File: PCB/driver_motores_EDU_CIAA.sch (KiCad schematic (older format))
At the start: 37 parts, among them P1 CONN_01X02, P2 CONN_01X04, P3 CONN_01X05, P4 CONN_01X05, Q1 AOD417, U1 PCA9685-TSSOP, U2 24C32, U3 TB6612FNG, U4 TB6612FNG

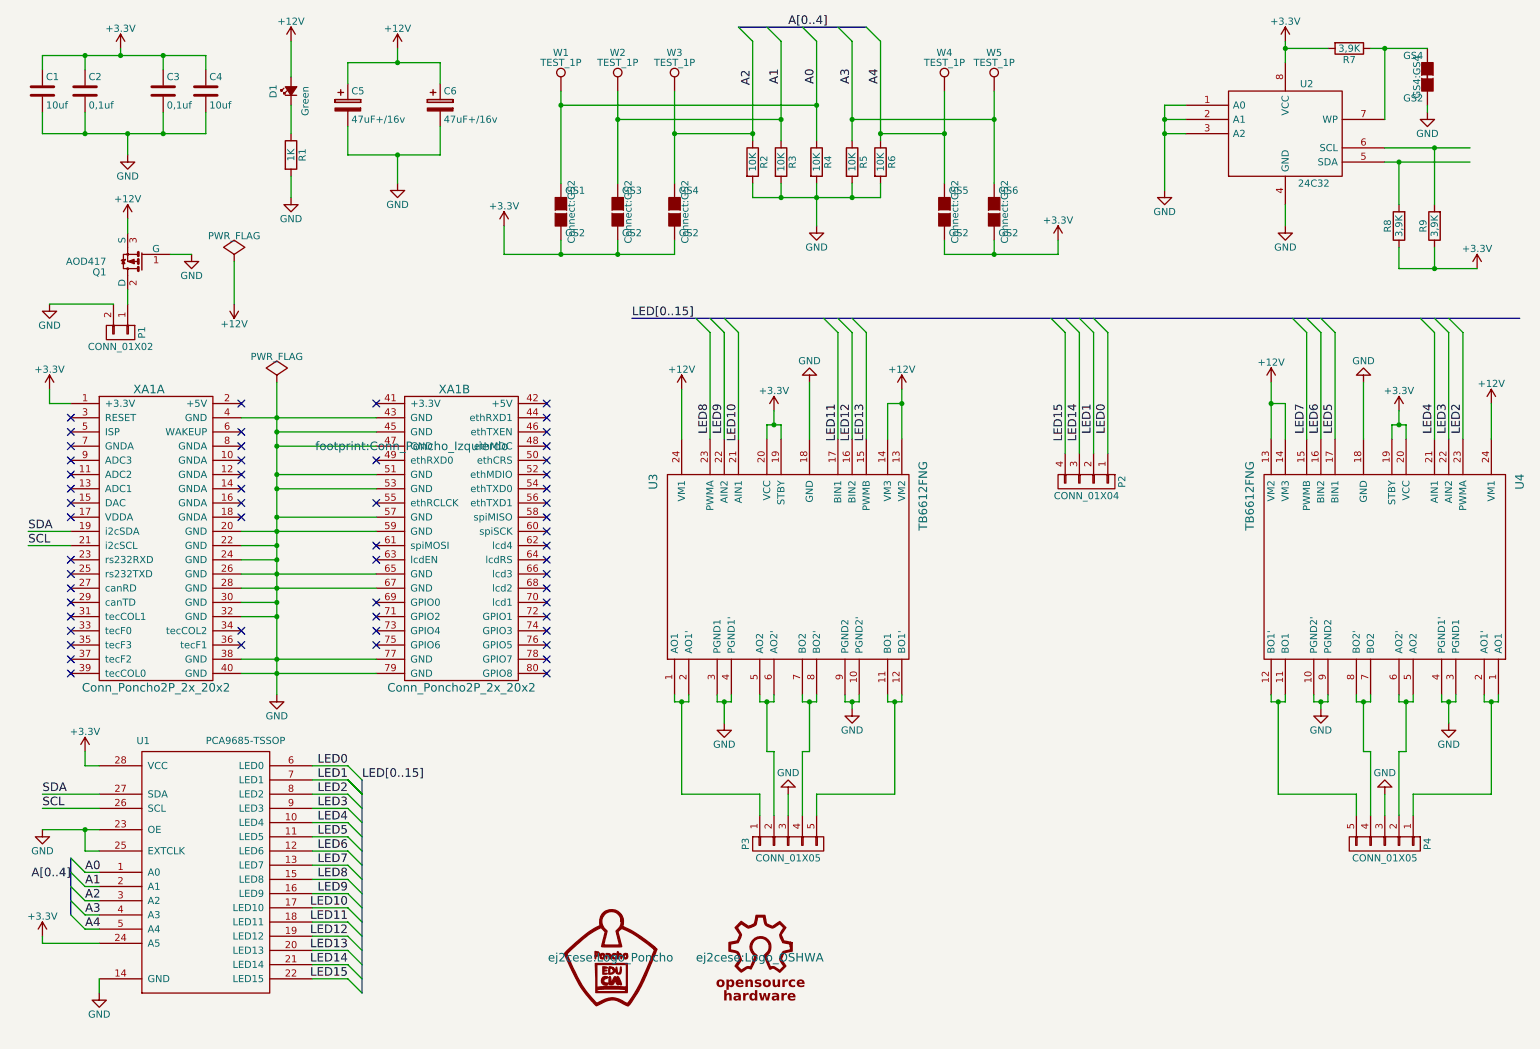
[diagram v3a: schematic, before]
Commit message: se borran las carpetas sobrantes, completa el rotulo, se corrige el esquematico, se agrega serigrafia, se agrega tabla con las grillas
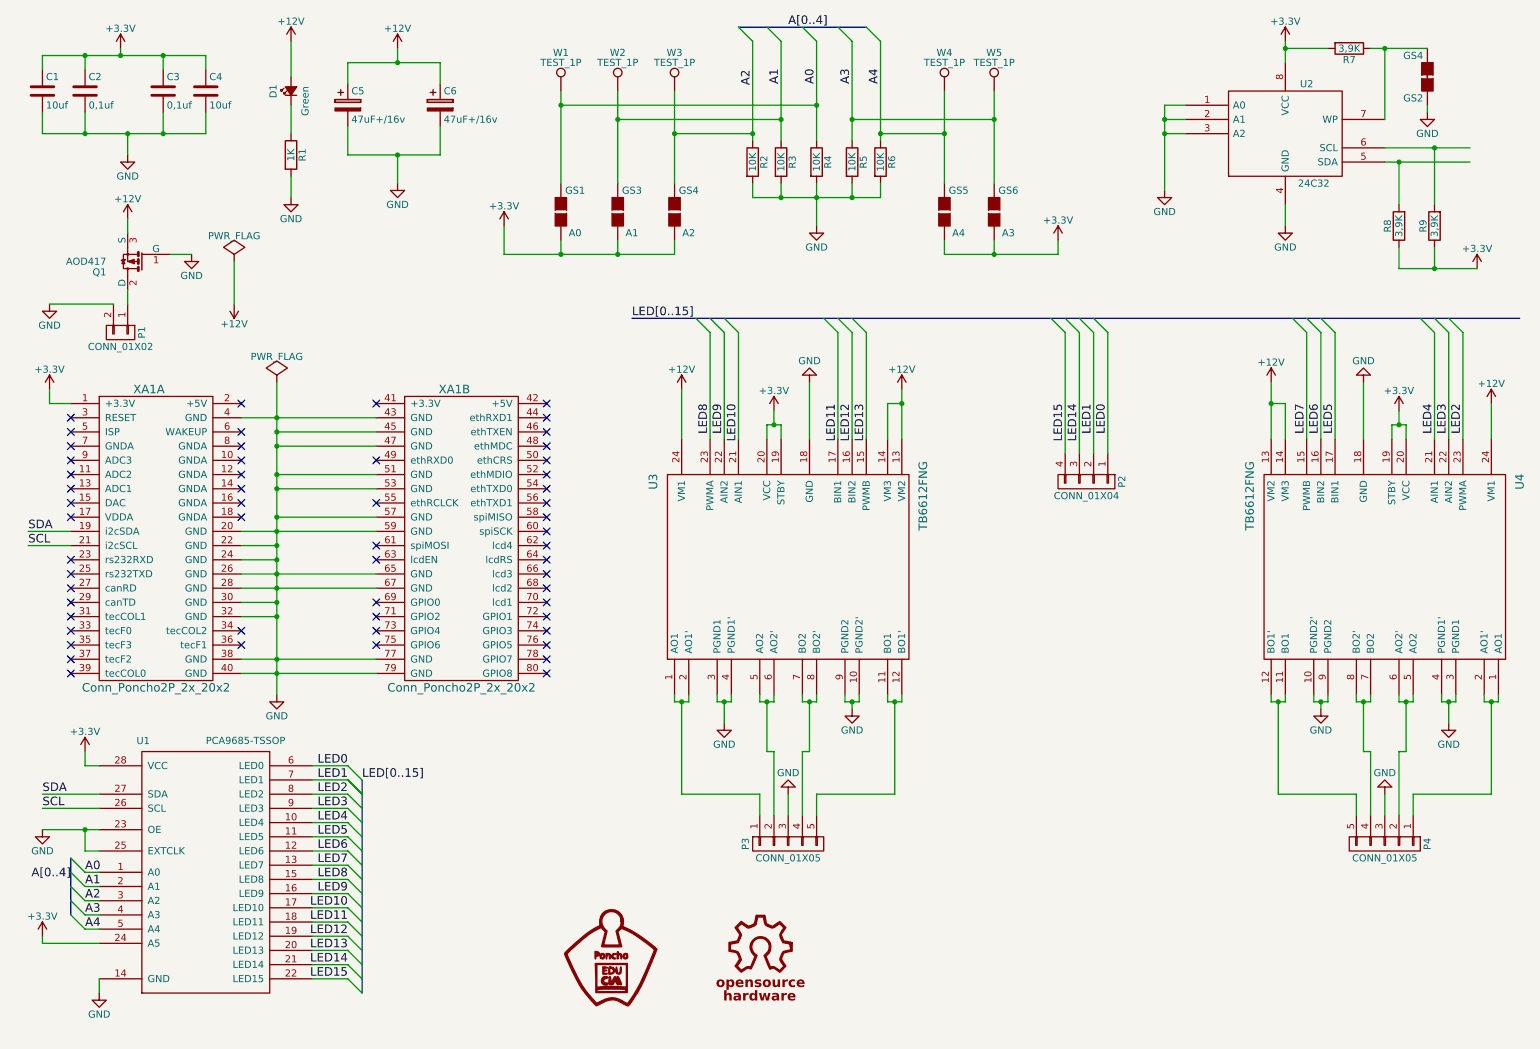
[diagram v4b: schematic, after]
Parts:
- GS1: value GS2 -> A0
- GS3: value GS2 -> A1
- GS4: value GS2 -> A2
- GS5: value GS2 -> A4
- GS6: value GS2 -> A3
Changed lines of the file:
@@
 encoding utf-8
 Sheet 1 1
-Title "Poncho punete H por i2C "
-Date "2016-12-13"
-Rev "1.2"
+Title "Poncho puente H por i2C "
+Date "2016-12-22"
+Rev "1.3"
 Comp "Martinez Horacio"
 Comment1 "Revisor: Guillermo Evangelista"
-Comment2 ""
+Comment2 "https://github.com/martinezhoracio/tp_KiCad_2016"
 Comment3 ""
 Comment4 ""
@@
 F 0 "GS2" H 10500 1100 50  0000 C CNN
 F 1 "GS4" H 10500 801 50  0000 C CNN
-F 2 "GS4:GS4" V 10474 950 50  0000 C CNN
+F 2 "GS4:GS4" V 10474 950 50  0001 C CNN
 F 3 "" H 10400 950 50  0000 C CNN
 	1    10400 950
@@
 P 4300 1900
 F 0 "GS1" H 4400 2050 50  0000 C CNN
-F 1 "GS2" H 4400 1751 50  0000 C CNN
-F 2 "Connect:GS2" V 4374 1900 50  0000 C CNN
+F 1 "A0" H 4400 1751 50  0000 C CNN
+F 2 "Connect:GS2" V 4374 1900 50  0001 C CNN
 F 3 "" H 4300 1900 50  0000 C CNN
 	1    4300 1900
@@
 P 4700 1900
 F 0 "GS3" H 4800 2050 50  0000 C CNN
-F 1 "GS2" H 4800 1751 50  0000 C CNN
-F 2 "Connect:GS2" V 4774 1900 50  0000 C CNN
+F 1 "A1" H 4800 1751 50  0000 C CNN
+F 2 "Connect:GS2" V 4774 1900 50  0001 C CNN
 F 3 "" H 4700 1900 50  0000 C CNN
 	1    4700 1900
@@
 P 5100 1900
 F 0 "GS4" H 5200 2050 50  0000 C CNN
-F 1 "GS2" H 5200 1751 50  0000 C CNN
-F 2 "Connect:GS2" V 5174 1900 50  0000 C CNN
+F 1 "A2" H 5200 1751 50  0000 C CNN
+F 2 "Connect:GS2" V 5174 1900 50  0001 C CNN
 F 3 "" H 5100 1900 50  0000 C CNN
 	1    5100 1900
@@
 P 7000 1900
 F 0 "GS5" H 7100 2050 50  0000 C CNN
-F 1 "GS2" H 7100 1751 50  0000 C CNN
-F 2 "Connect:GS2" V 7074 1900 50  0000 C CNN
+F 1 "A4" H 7100 1751 50  0000 C CNN
+F 2 "Connect:GS2" V 7074 1900 50  0001 C CNN
 F 3 "" H 7000 1900 50  0000 C CNN
 	1    7000 1900
@@
 P 7350 1900
 F 0 "GS6" H 7450 2050 50  0000 C CNN
-F 1 "GS2" H 7450 1751 50  0000 C CNN
-F 2 "Connect:GS2" V 7424 1900 50  0000 C CNN
+F 1 "A3" H 7450 1751 50  0000 C CNN
+F 2 "Connect:GS2" V 7424 1900 50  0001 C CNN
 F 3 "" H 7350 1900 50  0000 C CNN
 	1    7350 1900
@@
 F 0 "#G1" H 4600 6750 60  0001 C CNN
 F 1 "Logo_Poncho" H 4850 6750 60  0001 C CNN
-F 2 "ej2cese:Logo_Poncho" H 4650 7150 60  0000 C CNN
+F 2 "ej2cese:Logo_Poncho" H 4650 7150 60  0001 C CNN
 F 3 "" H 4650 7150 60  0000 C CNN
 	1    4650 7150
@@
 F 0 "#G2" H 5670 7550 60  0001 C CNN
 F 1 "OSHWA" H 5700 7453 60  0001 C CNN
-F 2 "ej2cese:Logo_OSHWA" H 5700 7150 60  0000 C CNN
+F 2 "ej2cese:Logo_OSHWA" H 5700 7150 60  0001 C CNN
 F 3 "" H 5700 7150 60  0000 C CNN
 	1    5700 7150
@@
 F 0 "XA1" H 3550 3950 60  0000 C CNN
 F 1 "Conn_Poncho2P_2x_20x2" H 3600 1850 60  0000 C CNN
-F 2 "footprint:Conn_Poncho_Izquierdo" H 3250 3550 60  0000 C CNN
+F 2 "footprint:Conn_Poncho_Izquierdo" H 3250 3550 60  0001 C CNN
 F 3 "" H 3250 3550 60  0000 C CNN
 F 4 "952-1387-ND" H 3250 3550 60  0001 C CNN "digikey#"
